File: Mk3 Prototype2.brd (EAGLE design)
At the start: 119.6 x 68 mm, 144 parts, among them IC1 TPD3E001DRL, IC2 TPS62082, IC3 STM32F401V, IC4 BQ2409X, IC6 CC3100MOD, IC7 BQ2970, J1 ZX62-AB-5PA(11), J2 ER-TFT024-3, J3 SWD_SHROUD, Q1 DMMT5401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

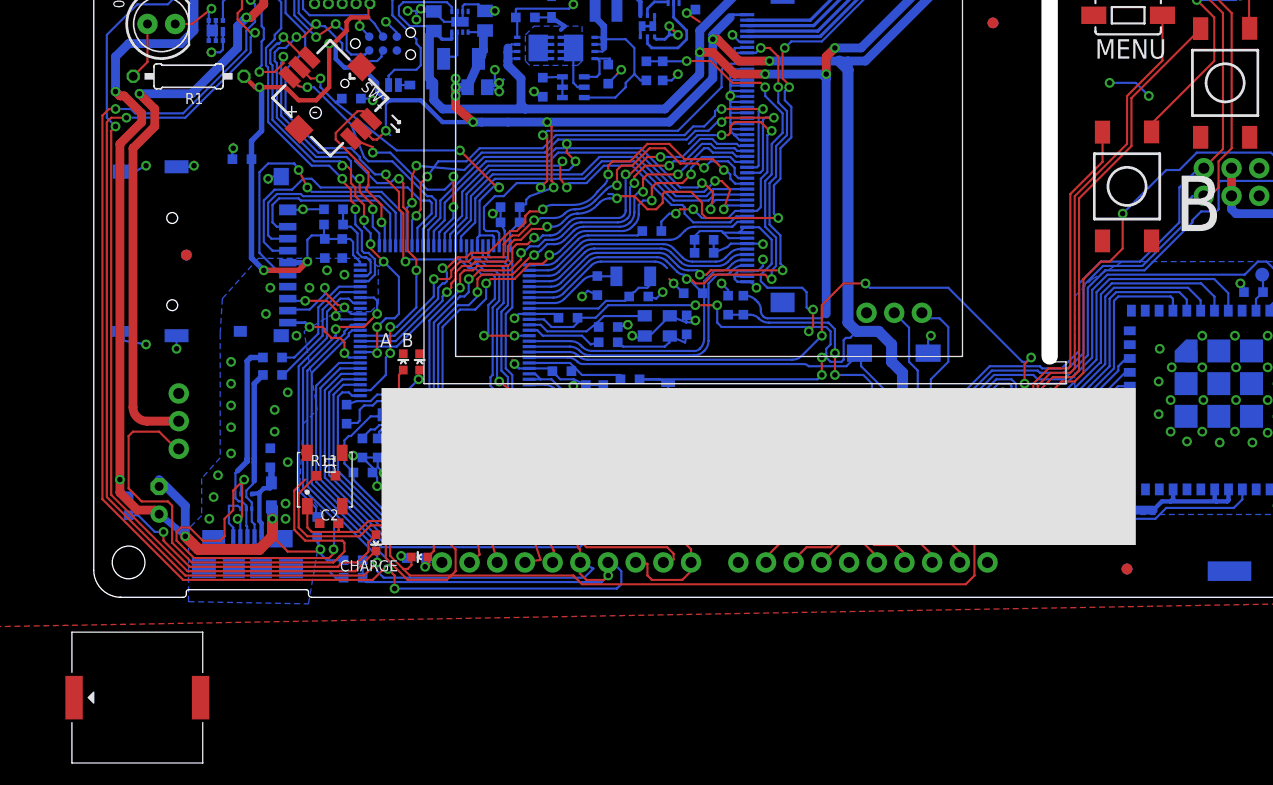
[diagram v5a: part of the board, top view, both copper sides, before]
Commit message: added imu
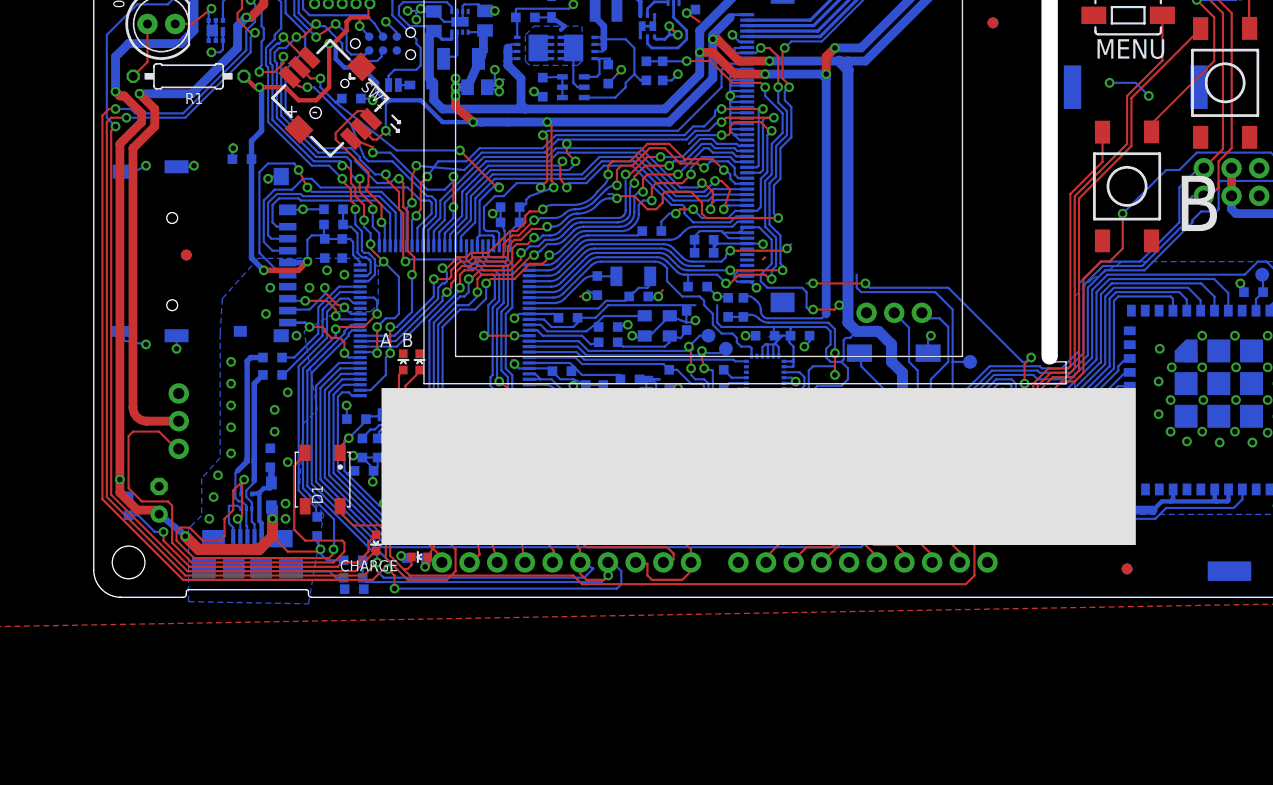
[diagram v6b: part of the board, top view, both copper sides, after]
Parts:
- added C28: 0603/10u/10V/X5R, TiLDA Mk3 Parts:C0603K-SMALL
- added C30: 0603/100n/10V/X5R, TiLDA Mk3 Parts:C0603K-SMALL
- added C31: 0603/4u7/10V/X5R, TiLDA Mk3 Parts:C0603K-SMALL
- added C32: 0603/220n/10V/X5R, TiLDA Mk3 Parts:C0603K-SMALL
- added IC5: LSM9DS0, TiLDA Mk3 Parts:LGA24
- added TP18, TP19, TP20: TPB1,27, TiLDA Mk3 Parts:B1,27
- moved SG1 107.4 mm to (95.6, 46.8), flipped to the bottom
- moved C18 21.5 mm to (52.8, 20.0)
- moved R11 10.7 mm to (23.9, 0.75), flipped to the bottom
- moved R14 8.22 mm to (31.0, 14.2), turned to 0 degrees
- moved C2 5.77 mm to (24.8, 11.6), flipped to the bottom
- moved C11 4.94 mm to (24.1, 16.4), turned to 180 degrees
- moved SJ2 2.04 mm to (50.7, 19.5)
- moved C13 1.71 mm to (33.0, 11.6)
- moved C33 0.72 mm to (55.4, 28.5), turned to 0 degrees
- moved C14 0.40 mm to (35.2, 12.2)
- moved C20 0.40 mm to (54.4, 25.4)
- moved C12 0.20 mm to (38.8, 14.8)
- moved D1 0.20 mm to (21.0, 10.8), turned to 270 degrees
- moved R3 0.20 mm to (59.6, 26.6)
- moved R4 0.20 mm to (58.2, 26.6)
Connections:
- net TIM10_CH1 renamed I2C_SCL
- net TIM11_CH1 renamed I2C_SDA
- removed net A5: TP7.P$1
- removed net LCD_ADC_X: IC3.15, J2.46
- removed net LCD_ADC_Y: IC3.16, J2.47
- removed net LCD_X: IC3.3, J2.44
- removed net LCD_Y: IC3.4, J2.45
- removed net N$14: LED1.K, Q3.1, Q3.2, Q3.5, Q3.6, Q3.EP1
- removed net N$4: C9.2, IC3.48
- removed net N$8: IC3.7
- new net ADC_IN: IC3.35, JP1.10
- new net FET_OUT: LED1.K, Q3.1, Q3.2, Q3.5, Q3.6, Q3.EP1, TP7.P$1
- new net IMU_IRQ1: IC3.17, IC5.12
- new net IMU_IRQ2: IC3.7, IC5.13
- new net IMU_SCL: IC3.15, IC5.21, TP19.TP
- new net IMU_SDA: IC3.16, IC5.24, TP18.TP
- new net N$16: C31.2, IC5.7
- new net N$18: C32.2, IC5.9
- new net N$19: C32.1, IC5.8
- new net PB11: C9.2, IC3.48, JP2.10
- net +3V3: now also C28.2, C30.2, IC5.15, IC5.16, IC5.17, IC5.18, IC5.19, IC5.20, JP1.1
- net ADC_VIN: now also IC3.18; no longer IC3.35
- net BOOT1: now also D1.4
- net CC_IRQ: now also IC3.3; no longer IC3.17
- net CC_RST: now also IC3.4, TP20.TP; no longer IC3.18
- net GND: now also C28.1, C30.1, C31.1, IC5.2, IC5.22, IC5.23, IC5.3, IC5.4, IC5.5, IC5.6
- net TIM1_CH4: no longer D1.4
- net V_UNREG: now also JP2.1
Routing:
- net IMU_SCL: track 0.00 -> 39.7 mm, vias 0 -> 2
- net IMU_SDA: track 0.00 -> 35.9 mm, vias 0 -> 2
- net ADC_IN: track 0.00 -> 32.2 mm
- net IMU_IRQ2: track 0.00 -> 27.3 mm
- net ADC_VIN: track 79.5 -> 52.4 mm, vias 4 -> 2
- net LCD_ADC_X: track 26.8 -> 0.00 mm
- net LCD_ADC_Y: track 26.7 -> 0.00 mm
- net LCD_Y: track 21.9 -> 0.00 mm
- net LCD_X: track 21.9 -> 0.00 mm
- net IMU_IRQ1: track 0.00 -> 20.3 mm
- net +3V3: track 536.3 -> 551.5 mm, vias 29 -> 26
- net N$8: track 14.0 -> 0.00 mm
- net PB11: track 0.00 -> 13.8 mm, vias 0 -> 1
- net GND: track 191.8 -> 203.9 mm, vias 118 -> 122
- net CC_RST: track 84.6 -> 96.2 mm
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
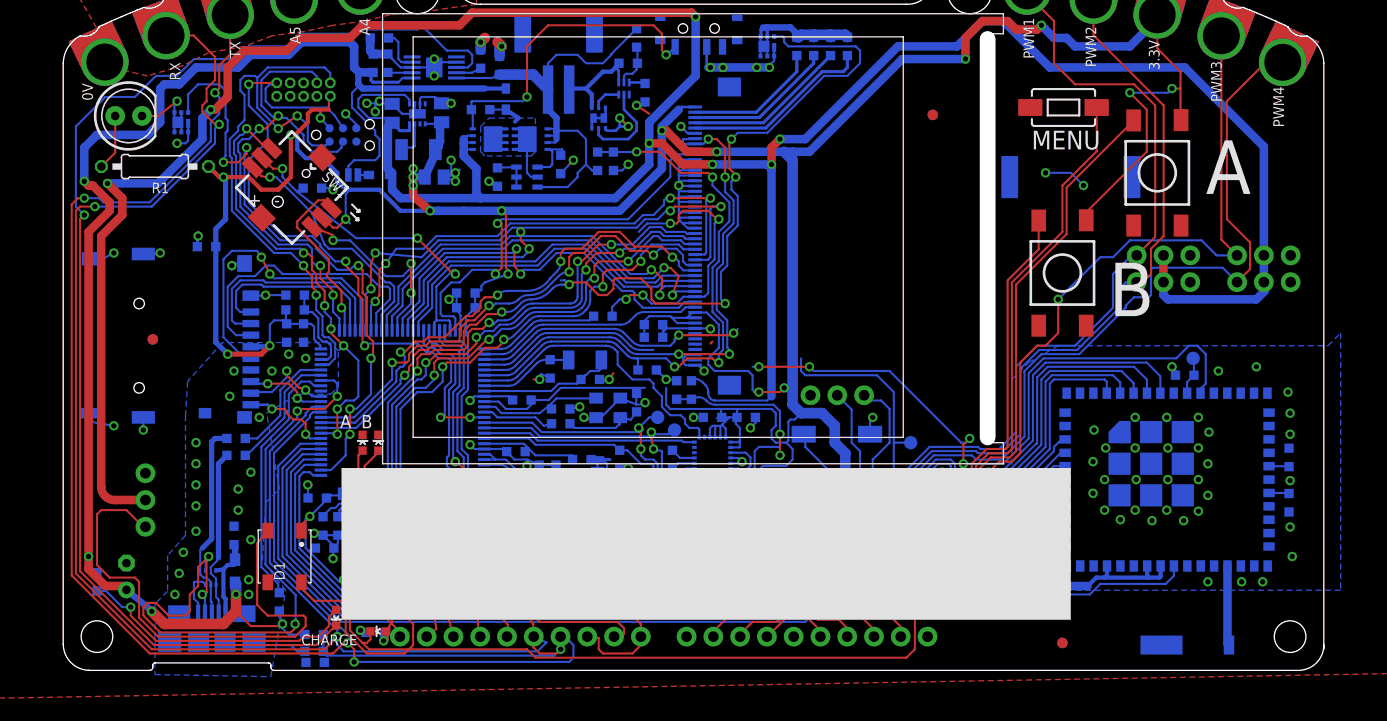
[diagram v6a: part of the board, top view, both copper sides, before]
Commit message: fixing outline
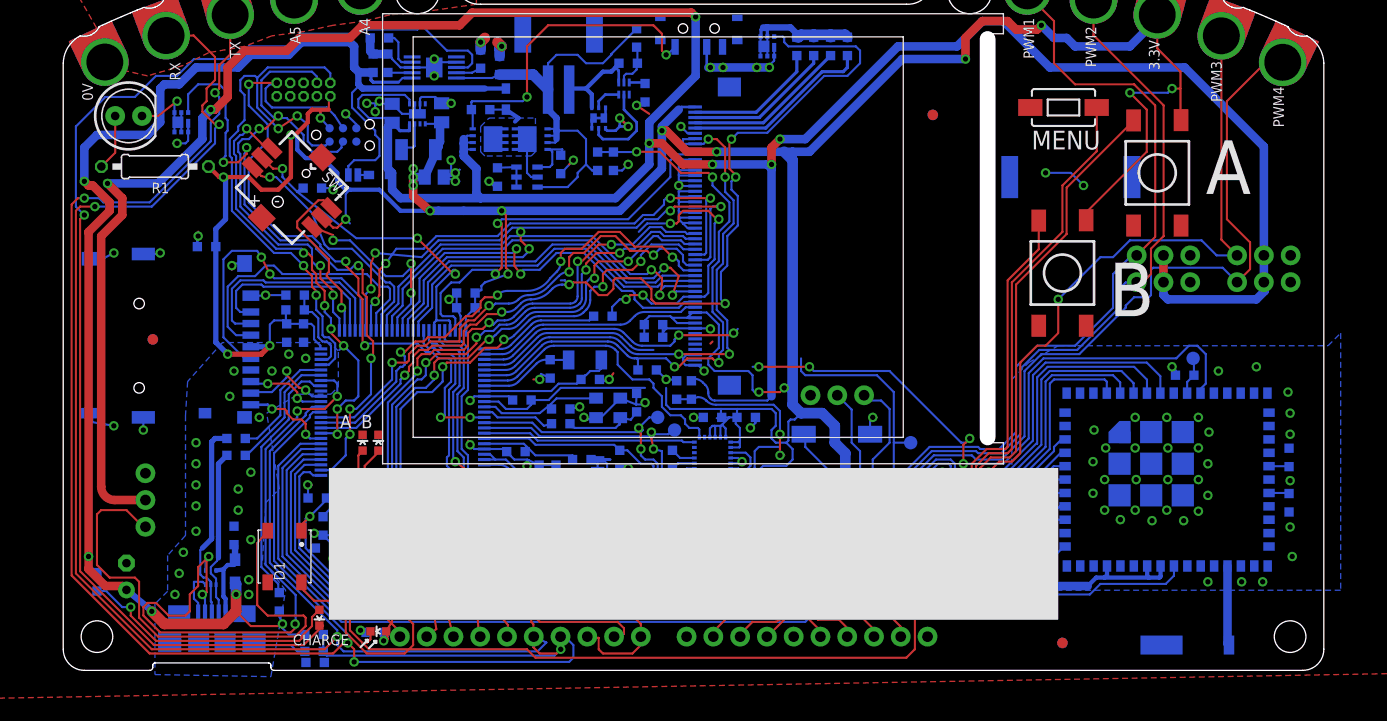
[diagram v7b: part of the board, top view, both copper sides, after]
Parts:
- moved LED5 1.60 mm to (24.3, 5.00)
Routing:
- net N$35: track 26.8 -> 25.6 mm
- net N$9: track 115.9 -> 115.0 mm
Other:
- outline, holes or cut-outs redrawn
- board text removed: "M. Brejza, LWK, parag0n"
- board text removed: "Powered by:"
- board text removed: "Tilda Mk3 Rev.1 Oct 2015"

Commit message: zero airwires
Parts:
- added R26: 0603/120/5%, TiLDA Mk3 Parts:C0603K-SMALL
- added TP21: TPB1,27, TiLDA Mk3 Parts:B1,27
- JP1, JP2: value M10NOSILK -> M11PTH; device TiLDA Mk3 Parts:1X10-NOSILK -> SparkFun-Connectors:1X11
- moved SG1 88.8 mm to (6.80, 44.8)
- moved FID2 30.1 mm to (84.8, 31.0)
- moved FID5 30.1 mm to (84.8, 31.0)
- moved R11 12.5 mm to (31.5, 10.7), turned to 0 degrees
- moved R1 6.40 mm to (15.0, 46.7), turned to 90 degrees
- moved LED4 6.32 mm to (23.7, 2.50), turned to 90 degrees
- moved R2 6.25 mm to (7.20, 3.60)
- moved R5 5.49 mm to (24.2, 2.60), turned to 90 degrees
- moved JP1 3.68 mm to (85.7, 3.20), flipped to the bottom, turned to 0 degrees
- moved LED5 3.04 mm to (21.4, 5.90), turned to 180 degrees
- moved C17 2.15 mm to (14.4, 38.2)
- moved R18 2.04 mm to (21.8, 3.00)
- moved R19 2.04 mm to (21.8, 1.40)
- moved U1 1.60 mm to (7.20, 33.2)
- moved FID3 1.44 mm to (9.30, 30.2)
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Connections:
- removed net A4: TP8.P$1
- removed net N$35: LED5.A, R2.1
- removed net TIM1_CH1: JP1.6
- removed net TIM4_CH2: IC3.60, Q8.3
- new net BUZZ: IC3.59, R26.2
- new net N$4: R26.1, SG1.P$1
- new net N$8: LED5.C, R2.2
- new net TIM17_CH1: IC3.98, Q8.3
- net +3V3: now also JP2.1, TP5.P$1; no longer S3.A2, S4.A2, TP6.P$1
- net ADC_IN: now also JP2.7; no longer JP1.10
- net CC_RST: now also IC3.2; no longer IC3.4
- net FET_OUT: now also TP1.P$1; no longer TP7.P$1
- net GND: now also JP1.11, JP2.11, S3.A2, S4.A2, S7.1, SG1.P$2, TP10.P$1; no longer TP5.P$1
- net I2C_SCL: now also JP2.4; no longer JP2.2
- net JOY_UP: now also IC3.58; no longer IC3.59
- net LCD_!RST: now also IC3.60; no longer IC3.98
- net N$9: now also R2.1; no longer LED5.C
- net PB11: now also JP1.7; no longer JP2.10
- net SDIO_SW: now also IC3.67; no longer IC3.58
- net SPI2_CLK: now also JP1.8; no longer JP2.7
- net SPI2_MISO: now also JP1.9; no longer JP2.8
- net SPI2_MOSI: now also JP1.10; no longer JP2.9
- net SPI2_NSS: now also JP1.6; no longer JP2.6
- net TEAR: now also IC3.4, TP21.TP; no longer IC3.2
- net TIM1_CH2: now also JP2.8; no longer JP1.7
- net TIM1_CH3: now also JP2.9; no longer JP1.8
- net TIM1_CH4: now also JP2.10; no longer JP1.9
- net TIM2_CH3: now also TP6.P$1; no longer TP10.P$1
- net USART6_RX: now also JP2.6, TP7.P$1; no longer JP2.5, TP1.P$1
- net USART6_TX: now also JP2.5; no longer JP2.4
- net VBUS: now also LED5.A; no longer R2.2
- net V_UNREG: now also JP2.2, TP8.P$1; no longer JP2.1
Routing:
- net V_UNREG: track 301.1 -> 396.8 mm, vias 7 -> 18
- net TIM4_CH2: track 91.8 -> 0.00 mm, vias 6 -> 0
- net BOOT1: track 90.2 -> 18.0 mm
- net TIM17_CH1: track 0.00 -> 57.6 mm, vias 0 -> 4
- net PB11: track 13.8 -> 57.1 mm
- net +3V3: track 551.5 -> 512.1 mm, vias 26 -> 30
- net TIM1_CH3: track 55.7 -> 22.1 mm
- net TIM1_CH2: track 55.3 -> 22.3 mm
- net LCD_!RST: track 39.3 -> 71.1 mm, vias 2 -> 6
- net TIM1_CH4: track 55.4 -> 24.0 mm
- net BUZZ: track 0.00 -> 29.9 mm, vias 0 -> 2
- net SPI2_NSS: track 35.1 -> 64.5 mm
- net SPI2_CLK: track 24.8 -> 53.1 mm
- net SPI2_MISO: track 30.4 -> 58.6 mm
- net SPI2_MOSI: track 31.1 -> 57.8 mm
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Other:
- board text added: "AP"
- board text added: "C"
- board text added: "D"
- board text added: "OD"
- board text added: "VBATT"
- board text removed: "A4"
- board text removed: "A5"
